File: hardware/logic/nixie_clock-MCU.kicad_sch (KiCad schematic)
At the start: 20 parts, among them J1 Conn_01x06_Pin, J2 Conn_01x04, SW1 SW_Push, SW2 SW_Push, U9 STM32F072RBTx, Y1 8 MHz

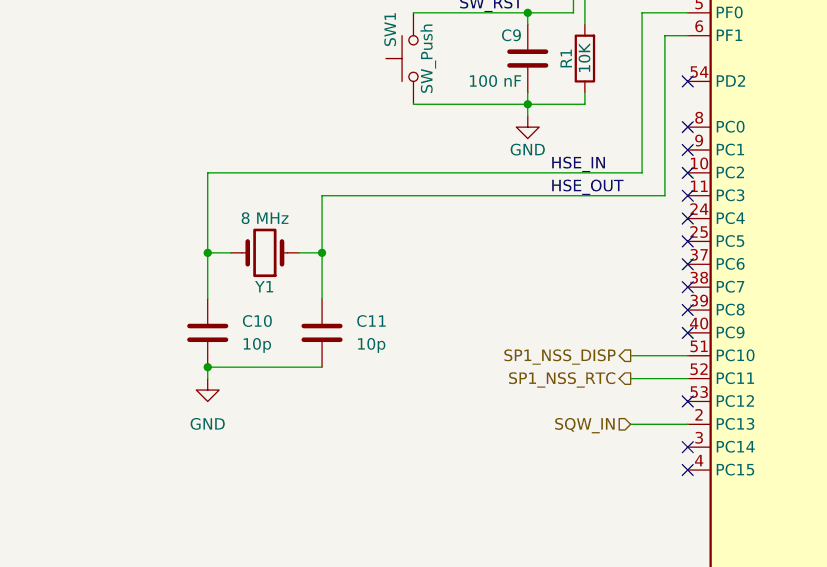
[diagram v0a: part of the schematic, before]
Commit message: Changed connectors to driver board, fixed oscillator connections
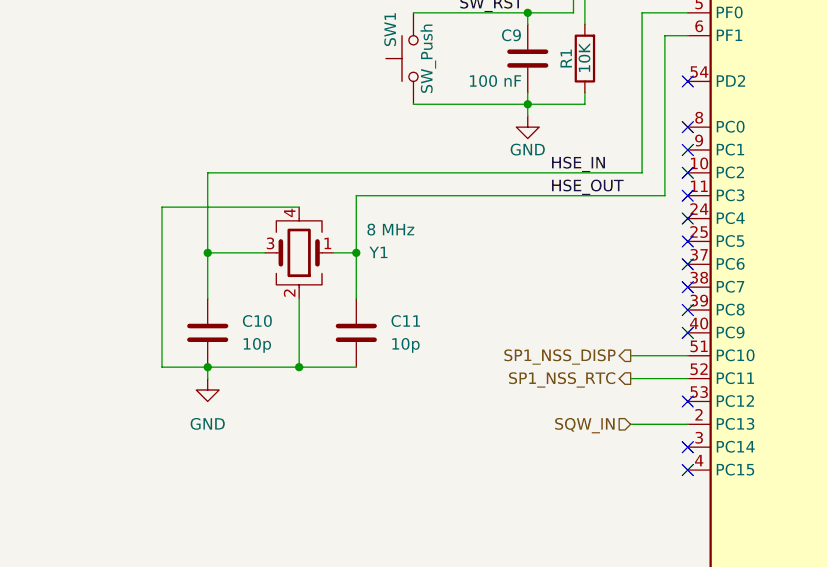
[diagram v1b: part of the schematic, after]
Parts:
- Y1: symbol Device:Crystal -> Device:Crystal_GND24
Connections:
- net GND: now also Y1.2, Y1.4
- net HSE_IN: now also Y1.3; no longer Y1.2
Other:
- moved on the sheet: C11
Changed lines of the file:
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@@
   (junction (at 167.64 31.75) (diameter 0) (color 0 0 0 0)
   )
+  (junction (at 86.36 101.6) (diameter 0) (color 0 0 0 0)
+  )
   (junction (at 205.74 24.13) (diameter 0) (color 0 0 0 0)
   )
@@
   (junction (at 198.12 31.75) (diameter 0) (color 0 0 0 0)
   )
-  (junction (at 88.9 88.9) (diameter 0) (color 0 0 0 0)
-  )
   (junction (at 167.64 24.13) (diameter 0) (color 0 0 0 0)
+  )
+  (junction (at 92.71 88.9) (diameter 0) (color 0 0 0 0)
   )
   (junction (at 182.88 31.75) (diameter 0) (color 0 0 0 0)
@@
     (stroke (width 0) (type default))
   )
-  (wire (pts (xy 88.9 82.55) (xy 88.9 88.9))
+  (wire (pts (xy 92.71 82.55) (xy 92.71 88.9))
     (stroke (width 0) (type default))
   )
@@
     (stroke (width 0) (type default))
   )
-  (wire (pts (xy 88.9 82.55) (xy 127 82.55))
+  (wire (pts (xy 92.71 82.55) (xy 127 82.55))
     (stroke (width 0) (type default))
   )
@@
     (stroke (width 0) (type default))
   )
+  (wire (pts (xy 71.12 101.6) (xy 76.2 101.6))
+    (stroke (width 0) (type default))
+  )
   (wire (pts (xy 167.64 31.75) (xy 175.26 31.75))
     (stroke (width 0) (type default))
@@
     (stroke (width 0) (type default))
   )
+  (wire (pts (xy 71.12 83.82) (xy 71.12 101.6))
+    (stroke (width 0) (type default))
+  )
   (wire (pts (xy 118.11 30.48) (xy 118.11 39.37))
     (stroke (width 0) (type default))
   )
+  (wire (pts (xy 86.36 101.6) (xy 92.71 101.6))
+    (stroke (width 0) (type default))
+  )
   (wire (pts (xy 39.37 179.07) (xy 44.45 179.07))
     (stroke (width 0) (type default))
@@
     (stroke (width 0) (type default))
   )
-  (wire (pts (xy 86.36 88.9) (xy 88.9 88.9))
+  (wire (pts (xy 90.17 88.9) (xy 92.71 88.9))
     (stroke (width 0) (type default))
   )
@@
     (stroke (width 0) (type default))
   )
+  (wire (pts (xy 86.36 83.82) (xy 71.12 83.82))
+    (stroke (width 0) (type default))
+  )
   (wire (pts (xy 127 82.55) (xy 127 64.77))
     (stroke (width 0) (type default))
@@
     (stroke (width 0) (type default))
   )
-  (wire (pts (xy 76.2 88.9) (xy 78.74 88.9))
+  (wire (pts (xy 76.2 88.9) (xy 82.55 88.9))
     (stroke (width 0) (type default))
   )
@@
     (stroke (width 0) (type default))
   )
-  (wire (pts (xy 76.2 101.6) (xy 88.9 101.6))
-    (stroke (width 0) (type default))
-  )
   (wire (pts (xy 76.2 102.87) (xy 76.2 101.6))
     (stroke (width 0) (type default))
@@
     (stroke (width 0) (type default))
   )
+  (wire (pts (xy 76.2 101.6) (xy 86.36 101.6))
+    (stroke (width 0) (type default))
+  )
+  (wire (pts (xy 86.36 93.98) (xy 86.36 101.6))
+    (stroke (width 0) (type default))
+  )
   (wire (pts (xy 125.73 24.13) (xy 144.78 24.13))
     (stroke (width 0) (type default))
@@
     (stroke (width 0) (type default))
   )
-  (wire (pts (xy 88.9 88.9) (xy 88.9 93.98))
+  (wire (pts (xy 92.71 88.9) (xy 92.71 93.98))
     (stroke (width 0) (type default))
   )
@@
     )
   )
-  (symbol (lib_id "Device:Crystal") (at 82.55 88.9 180) (unit 1)
-    (in_bom yes) (on_board yes) (dnp no)
-    (property "Reference" "Y1" (at 82.55 92.71 0)
+  (symbol (lib_id "Device:Crystal_GND24") (at 86.36 88.9 180) (unit 1)
+    (in_bom yes) (on_board yes) (dnp no)
+    (property "Reference" "Y1" (at 95.25 88.9 0)
       (effects (font (size 1.27 1.27)))
     )
-    (property "Value" "8 MHz" (at 82.55 85.09 0)
+    (property "Value" "8 MHz" (at 96.52 86.36 0)
       (effects (font (size 1.27 1.27)))
     )
-    (property "Footprint" "Crystal:Crystal_SMD_5032-4Pin_5.0x3.2mm" (at 82.55 88.9 0)
-      (effects (font (size 1.27 1.27)) hide)
-    )
-    (property "Datasheet" "http://www.abracon.com/Resonators/abm3b.pdf" (at 82.55 88.9 0)
-      (effects (font (size 1.27 1.27)) hide)
-    )
-    (property "Part Number" "ABM3B-8.000MHZ-10-1UT" (at 82.55 88.9 0)
+    (property "Footprint" "Crystal:Crystal_SMD_5032-4Pin_5.0x3.2mm" (at 86.36 88.9 0)
+      (effects (font (size 1.27 1.27)) hide)
+    )
+    (property "Datasheet" "~" (at 86.36 88.9 0)
+      (effects (font (size 1.27 1.27)) hide)
+    )
+    (property "Part Number" "ABM3B-8.000MHZ-10-1UT" (at 86.36 88.9 0)
       (effects (font (size 1.524 1.524)) hide)
     )
     (pin "2")
     (pin "1")
+    (pin "3")
+    (pin "4")
     (instances
       (project "nixie_clock"
@@
     )
   )
-  (symbol (lib_id "Device:C") (at 88.9 97.79 0) (unit 1)
+  (symbol (lib_id "Device:C") (at 92.71 97.79 0) (unit 1)
     (in_bom yes) (on_board yes) (dnp no) (fields_autoplaced)
-    (property "Reference" "C11" (at 92.71 96.52 0)
-      (effects (font (size 1.27 1.27)) (justify left))
-    )
-    (property "Value" "10p" (at 92.71 99.06 0)
-      (effects (font (size 1.27 1.27)) (justify left))
-    )
-    (property "Footprint" "Capacitor_SMD:C_0603_1608Metric_Pad1.08x0.95mm_HandSolder" (at 89.8652 101.6 0)
-      (effects (font (size 1.27 1.27)) hide)
-    )
-    (property "Datasheet" "~" (at 88.9 97.79 0)
-      (effects (font (size 1.27 1.27)) hide)
-    )
+    (property "Reference" "C11" (at 96.52 96.52 0)
+      (effects (font (size 1.27 1.27)) (justify left))
+    )
+    (property "Value" "10p" (at 96.52 99.06 0)
+      (effects (font (size 1.27 1.27)) (justify left))
+    )
+    (property "Footprint" "Capacitor_SMD:C_0603_1608Metric_Pad1.08x0.95mm_HandSolder" (at 93.6752 101.6 0)
+      (effects (font (size 1.27 1.27)) hide)
+    )
+    (property "Datasheet" "~" (at 92.71 97.79 0)
+      (effects (font (size 1.27 1.27)) hide)
+    )

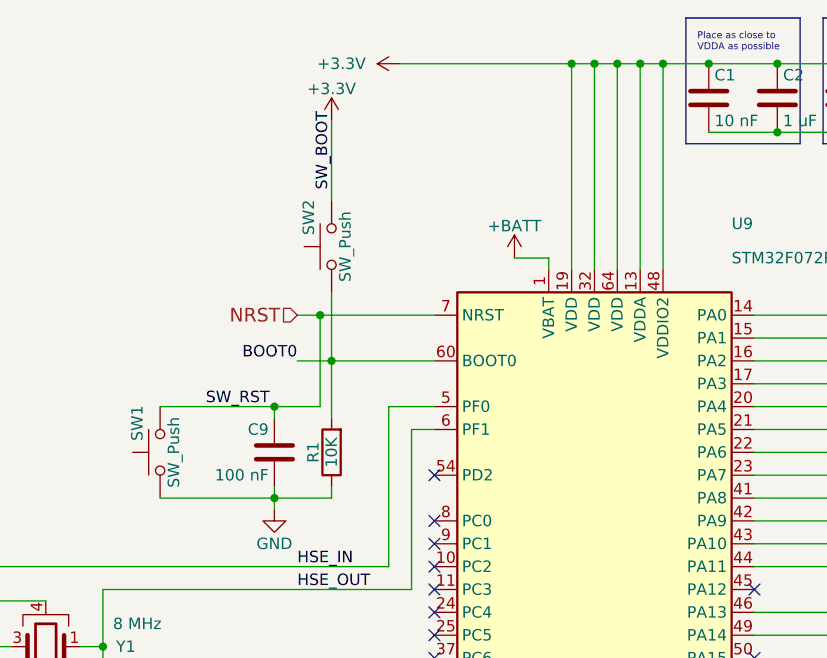
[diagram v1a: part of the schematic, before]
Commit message: Troubleshooting logic board design, begin component placement, fix positioning of board connectors
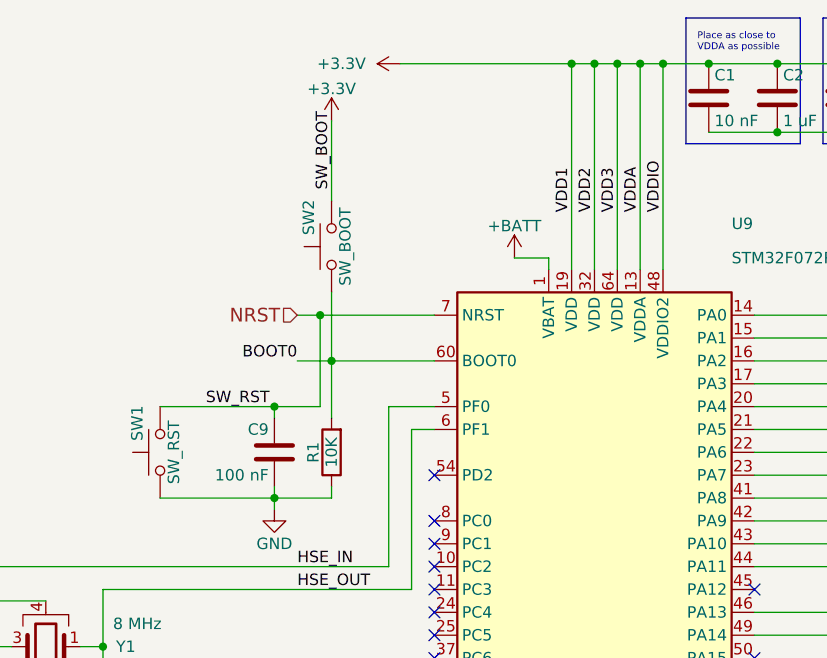
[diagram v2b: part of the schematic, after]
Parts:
- R1: footprint Resistor_SMD:R_0805_2012Metric -> Resistor_SMD:R_0603_1608Metric_Pad0.98x0.95mm_HandSolder
- SW1: value SW_Push -> SW_RST; footprint Button_Switch_SMD:SW_Push_1P1T_NO_CK_KSC6xxJ -> Button_Switch_SMD:SW_Push_1P1T_NO_CK_KMR2
- SW2: value SW_Push -> SW_BOOT
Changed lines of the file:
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@@
     (effects (font (size 1.27 1.27)) (justify right bottom))
+  )
+  (label "VDD1" (at 144.78 40.64 90) (fields_autoplaced)
+    (effects (font (size 1.27 1.27)) (justify left bottom))
   )
   (label "SWDIO" (at 176.53 85.09 0) (fields_autoplaced)
@@
     (effects (font (size 1.27 1.27)) (justify left bottom))
   )
+  (label "VDD3" (at 149.86 40.64 90) (fields_autoplaced)
+    (effects (font (size 1.27 1.27)) (justify left bottom))
+  )
   (label "HSE_IN" (at 114.3 80.01 0) (fields_autoplaced)
     (effects (font (size 1.27 1.27)) (justify left bottom))
@@
     (effects (font (size 1.27 1.27)) (justify right bottom))
   )
+  (label "VDDA" (at 152.4 40.64 90) (fields_autoplaced)
+    (effects (font (size 1.27 1.27)) (justify left bottom))
+  )
   (label "RXD" (at 87.63 185.42 180) (fields_autoplaced)
     (effects (font (size 1.27 1.27)) (justify right bottom))
   )
+  (label "VDD2" (at 147.32 40.64 90) (fields_autoplaced)
+    (effects (font (size 1.27 1.27)) (justify left bottom))
+  )
+  (label "VDDIO" (at 154.94 40.64 90) (fields_autoplaced)
+    (effects (font (size 1.27 1.27)) (justify left bottom))
+  )
   (label "SW_RST" (at 104.14 62.23 0) (fields_autoplaced)
     (effects (font (size 1.27 1.27)) (justify left bottom))
@@
       (effects (font (size 1.27 1.27)) (justify left))
     )
-    (property "Value" "SW_Push" (at 119.634 44.45 0)
+    (property "Value" "SW_BOOT" (at 119.634 44.45 0)
       (effects (font (size 1.27 1.27)))
     )
@@
       (effects (font (size 1.27 1.27)))
     )
-    (property "Footprint" "Resistor_SMD:R_0805_2012Metric" (at 119.888 67.31 90)
+    (property "Footprint" "Resistor_SMD:R_0603_1608Metric_Pad0.98x0.95mm_HandSolder" (at 119.888 67.31 90)
       (effects (font (size 1.27 1.27)) hide)
     )
@@
       (effects (font (size 1.27 1.27)) (justify left))
     )
-    (property "Value" "SW_Push" (at 100.584 67.31 0)
-      (effects (font (size 1.27 1.27)))
-    )
-    (property "Footprint" "Button_Switch_SMD:SW_Push_1P1T_NO_CK_KSC6xxJ" (at 93.98 67.31 0)
-      (effects (font (size 1.27 1.27)) hide)
-    )
+    (property "Value" "SW_RST" (at 100.584 67.31 0)
+      (effects (font (size 1.27 1.27)))
+    )
+    (property "Footprint" "Button_Switch_SMD:SW_Push_1P1T_NO_CK_KMR2" (at 93.98 67.31 0)
+      (effects (font (size 1.27 1.27)) hide)
+    )
